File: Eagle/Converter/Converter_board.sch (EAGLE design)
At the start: 9 parts

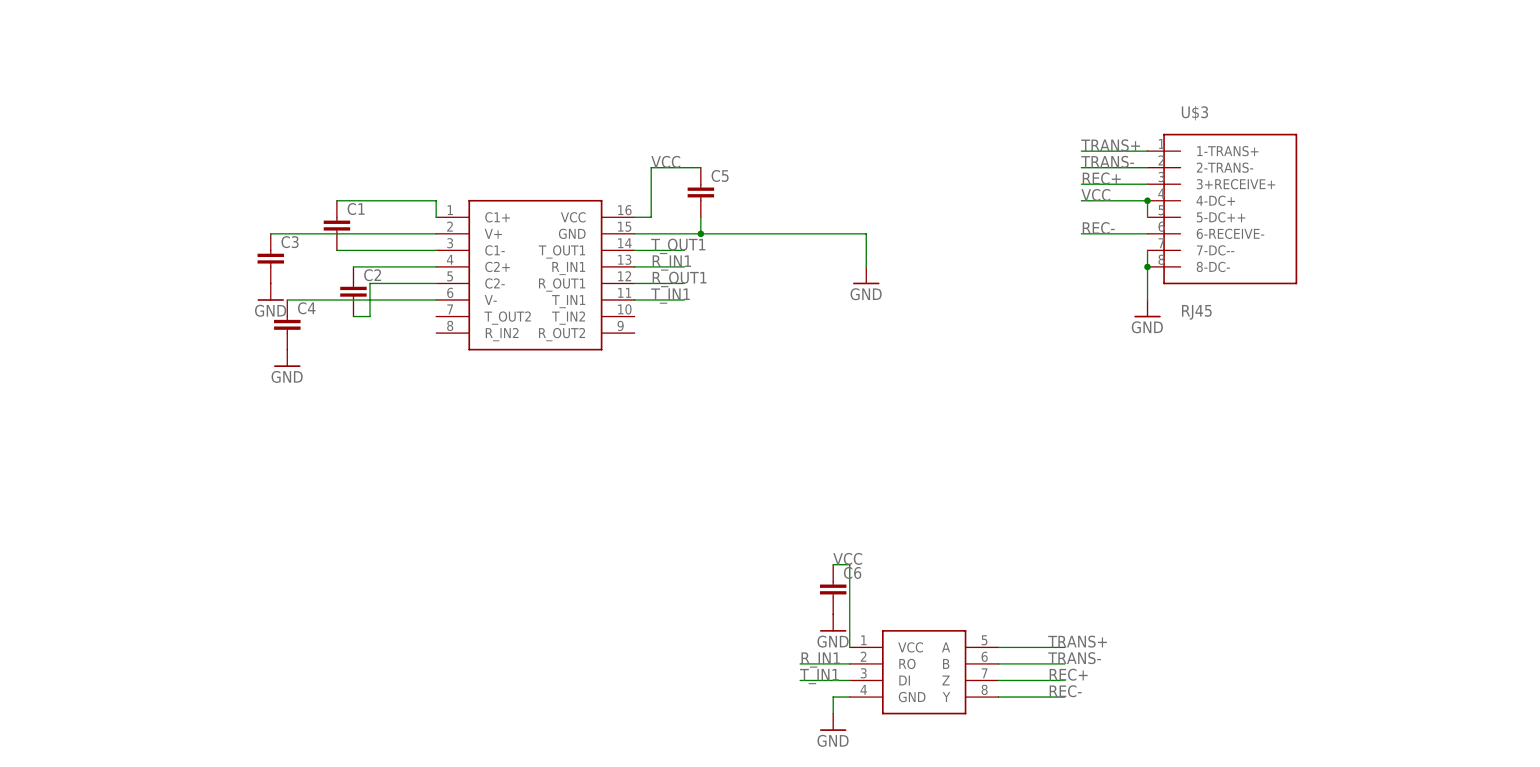
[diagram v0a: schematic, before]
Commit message: Added all parts needed
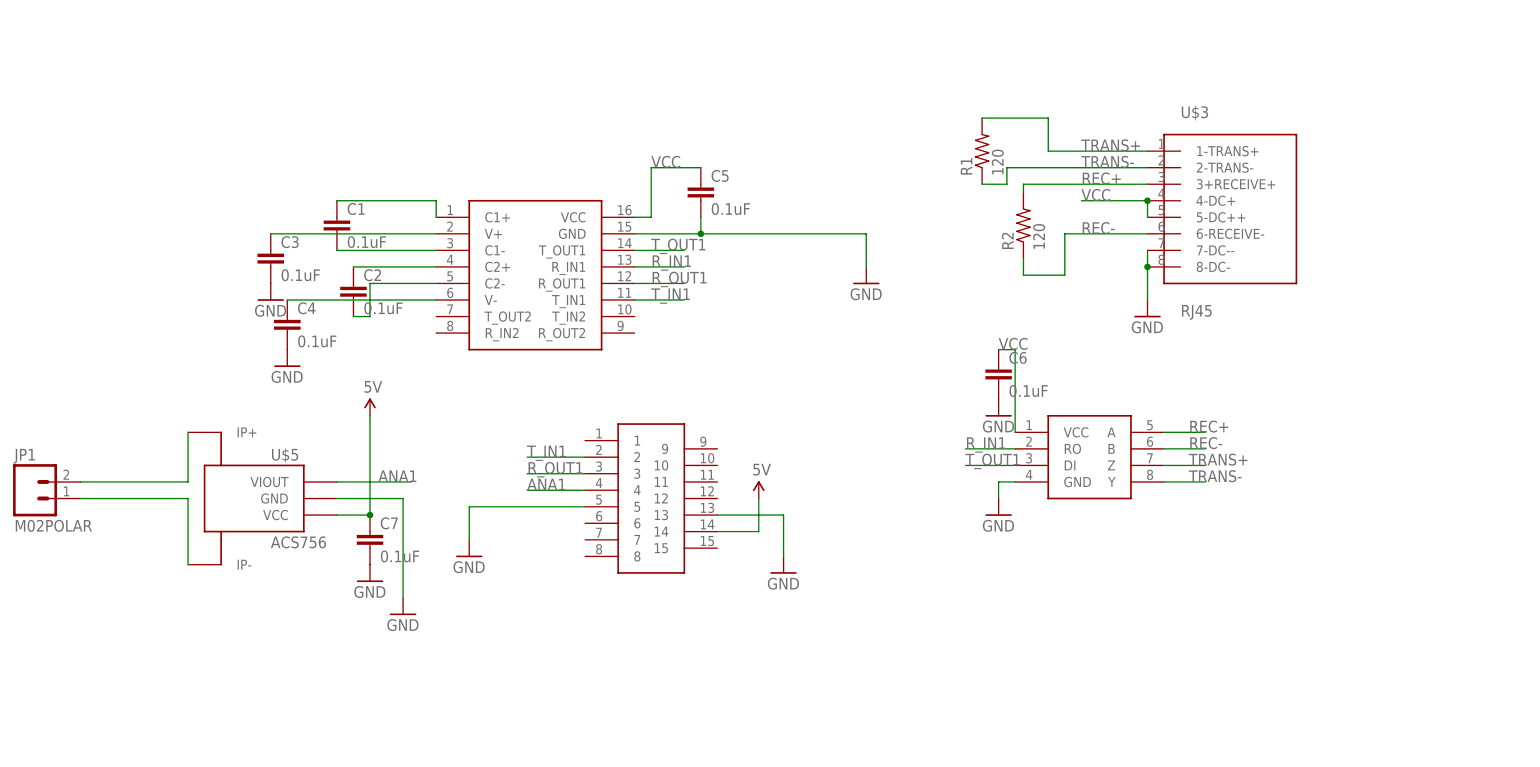
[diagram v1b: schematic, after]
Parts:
- added C7: 0.1uF, SparkFun-Capacitors:CAP1206
- added JP1: M02POLAR, SparkFun-Connectors:M02POLAR
- added R1, R2: 120, SparkFun-Passives:RESISTOR1206
- added U$4: DB15, MRDT-LIB2014:DB15
- added U$5: ACS756, MRDT-2015-BMS:ACS770
- C1, C2, C3, C4, C5, C6: value (none) -> 0.1uF
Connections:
- new net ANA1: U$4.4, U$5.VIOUT
- new net N$7: JP1.2, U$5.IP+
- new net N$9: JP1.1, U$5.IP-
- net GND: now also C7.2, U$4.13, U$4.5, U$5.GND
- net REC+: now also R2.2, U$1.A; no longer U$1.Z
- net REC-: now also R2.1, U$1.B; no longer U$1.Y
- net R_OUT1: now also U$4.3
- net TRANS+: now also R1.2, U$1.Z; no longer U$1.A
- net TRANS-: now also R1.1, U$1.Y; no longer U$1.B
- net T_IN1: now also U$4.2; no longer U$1.DI
- net T_OUT1: now also U$1.DI
- net VCC: now also C7.1, U$4.14, U$5.VCC
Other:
- moved on the sheet: C6

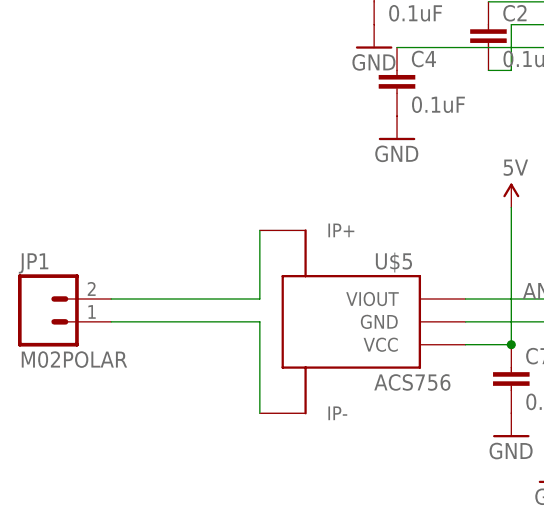
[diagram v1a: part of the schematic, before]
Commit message: Finished Schematic, Setup Board Layout. Waiting to hear final decision on Torque control.
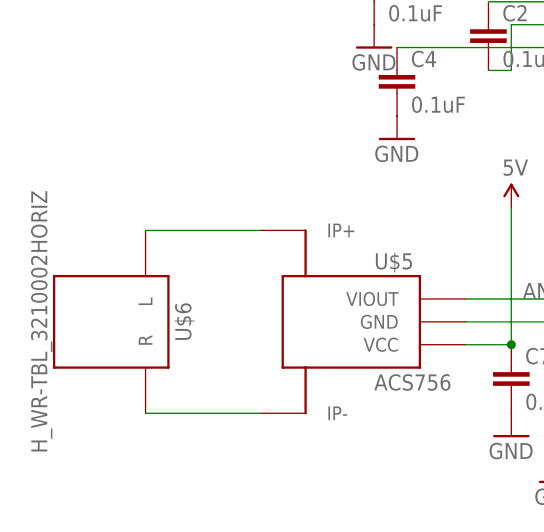
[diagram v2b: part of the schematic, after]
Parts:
- removed JP1: M02POLAR, SparkFun-Connectors:M02POLAR
- added U$6: H_WR-TBL_3210002HORIZ, MRDT-2015-PowerBoard:H_WR-TBL_3210002HORIZ
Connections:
- removed net N$9: JP1.1, U$5.IP-
- new net N$8: U$5.IP-, U$6.R
- net N$7: now also U$6.L; no longer JP1.2
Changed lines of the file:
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@@
 <part name="GND9" library="SparkFun-Aesthetics" deviceset="GND" device=""/>
 <part name="VCC1" library="SparkFun-Aesthetics" deviceset="5V" device=""/>
-<part name="JP1" library="SparkFun-Connectors" deviceset="M02" device="POLAR"/>
 <part name="R1" library="SparkFun-Passives" deviceset="RESISTOR" device="1206" value="120"/>
 <part name="R2" library="SparkFun-Passives" deviceset="RESISTOR" device="1206" value="120"/>
 <part name="C7" library="SparkFun-Capacitors" deviceset="CAP" device="1206" value="0.1uF"/>
 <part name="GND10" library="SparkFun-Aesthetics" deviceset="GND" device=""/>
+<part name="U$6" library="MRDT-2015-PowerBoard" deviceset="H_WR-TBL_32*1*0002" device="HORIZ"/>
 </parts>
 <sheets>
@@
 <instance part="GND9" gate="1" x="-15.24" y="45.72"/>
 <instance part="VCC1" gate="G$1" x="-20.32" y="76.2"/>
-<instance part="JP1" gate="G$1" x="-72.39" y="63.5"/>
 <instance part="R1" gate="G$1" x="73.66" y="116.84" rot="R90"/>
 <instance part="R2" gate="G$1" x="80.01" y="105.41" rot="R90"/>
 <instance part="C7" gate="G$1" x="-20.32" y="55.88"/>
 <instance part="GND10" gate="1" x="-20.32" y="50.8"/>
+<instance part="U$6" gate="G$1" x="-63.5" y="63.5" rot="R270"/>
 </instances>
 <busses>
@@
 <net name="N$7" class="0">
 <segment>
-<pinref part="JP1" gate="G$1" pin="2"/>
 <pinref part="U$5" gate="G$1" pin="IP+"/>
-<wire x1="-64.77" y1="66.04" x2="-48.26" y2="66.04" width="0.1524" layer="91"/>
-<wire x1="-48.26" y1="66.04" x2="-48.26" y2="73.66" width="0.1524" layer="91"/>
-</segment>
-</net>
-<net name="N$9" class="0">
-<segment>
-<pinref part="JP1" gate="G$1" pin="1"/>
+<wire x1="-48.26" y1="73.66" x2="-60.96" y2="73.66" width="0.1524" layer="91"/>
+<pinref part="U$6" gate="G$1" pin="L"/>
+</segment>
+</net>
+<net name="N$8" class="0">
+<segment>
 <pinref part="U$5" gate="G$1" pin="IP-"/>
-<wire x1="-64.77" y1="63.5" x2="-48.26" y2="63.5" width="0.1524" layer="91"/>
-<wire x1="-48.26" y1="63.5" x2="-48.26" y2="53.34" width="0.1524" layer="91"/>
-</segment>
-</net>
+<wire x1="-48.26" y1="53.34" x2="-60.96" y2="53.34" width="0.1524" layer="91"/>
+<pinref part="U$6" gate="G$1" pin="R"/>
+</segment>
+</net>

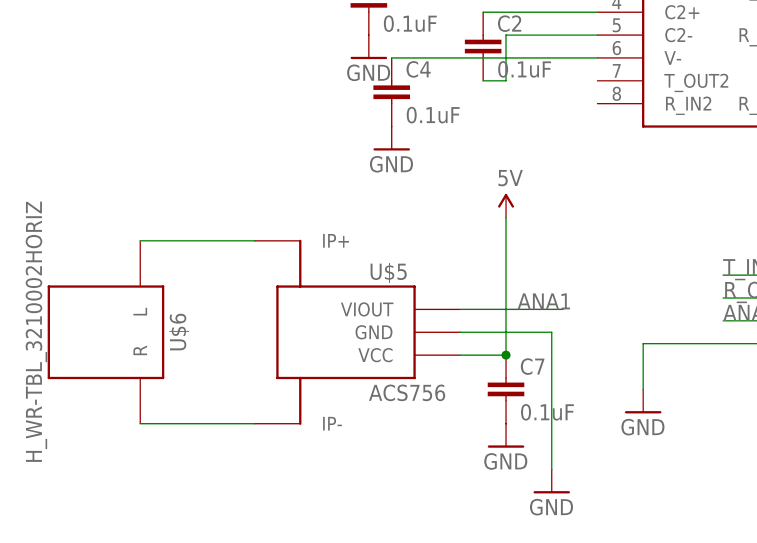
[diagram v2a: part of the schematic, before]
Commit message: Removed the Current Sensor. No more Torque control.
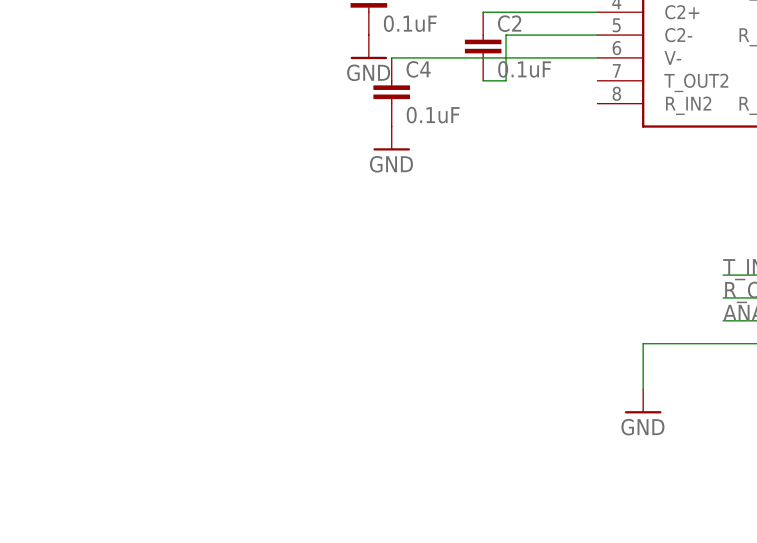
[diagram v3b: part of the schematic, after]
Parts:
- removed C7: 0.1uF, SparkFun-Capacitors:CAP1206
- removed U$5: ACS756, MRDT-2015-BMS:ACS770
- removed U$6: H_WR-TBL_3210002HORIZ, MRDT-2015-PowerBoard:H_WR-TBL_3210002HORIZ
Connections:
- removed net N$7: U$5.IP+, U$6.L
- removed net N$8: U$5.IP-, U$6.R
- net ANA1: no longer U$5.VIOUT
- net GND: no longer C7.2, U$5.GND
- net VCC: no longer C7.1, U$5.VCC
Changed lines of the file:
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@@
 <part name="GND8" library="SparkFun-Aesthetics" deviceset="GND" device=""/>
 <part name="VCC" library="SparkFun-Aesthetics" deviceset="5V" device=""/>
-<part name="U$5" library="MRDT-2015-BMS" deviceset="ACS770" device="" value="ACS756"/>
-<part name="GND9" library="SparkFun-Aesthetics" deviceset="GND" device=""/>
-<part name="VCC1" library="SparkFun-Aesthetics" deviceset="5V" device=""/>
 <part name="R1" library="SparkFun-Passives" deviceset="RESISTOR" device="1206" value="120"/>
 <part name="R2" library="SparkFun-Passives" deviceset="RESISTOR" device="1206" value="120"/>
-<part name="C7" library="SparkFun-Capacitors" deviceset="CAP" device="1206" value="0.1uF"/>
-<part name="GND10" library="SparkFun-Aesthetics" deviceset="GND" device=""/>
-<part name="U$6" library="MRDT-2015-PowerBoard" deviceset="H_WR-TBL_32*1*0002" device="HORIZ"/>
 </parts>
 <sheets>
@@
 <instance part="GND8" gate="1" x="-5.08" y="54.61"/>
 <instance part="VCC" gate="G$1" x="39.37" y="63.5"/>
-<instance part="U$5" gate="G$1" x="-38.1" y="63.5"/>
-<instance part="GND9" gate="1" x="-15.24" y="45.72"/>
-<instance part="VCC1" gate="G$1" x="-20.32" y="76.2"/>
 <instance part="R1" gate="G$1" x="73.66" y="116.84" rot="R90"/>
 <instance part="R2" gate="G$1" x="80.01" y="105.41" rot="R90"/>
-<instance part="C7" gate="G$1" x="-20.32" y="55.88"/>
-<instance part="GND10" gate="1" x="-20.32" y="50.8"/>
-<instance part="U$6" gate="G$1" x="-63.5" y="63.5" rot="R270"/>
 </instances>
 <busses>
@@
 <pinref part="GND8" gate="1" pin="GND"/>
 </segment>
-<segment>
-<pinref part="U$5" gate="G$1" pin="GND"/>
-<wire x1="-25.4" y1="63.5" x2="-15.24" y2="63.5" width="0.1524" layer="91"/>
-<wire x1="-15.24" y1="63.5" x2="-15.24" y2="48.26" width="0.1524" layer="91"/>
-<pinref part="GND9" gate="1" pin="GND"/>
-</segment>
-<segment>
-<pinref part="C7" gate="G$1" pin="2"/>
-<pinref part="GND10" gate="1" pin="GND"/>
-</segment>
 </net>
 <net name="VCC" class="0">
@@
 <wire x1="39.37" y1="58.42" x2="39.37" y2="63.5" width="0.1524" layer="91"/>
 <pinref part="VCC" gate="G$1" pin="5V"/>
-</segment>
-<segment>
-<pinref part="U$5" gate="G$1" pin="VCC"/>
-<wire x1="-25.4" y1="60.96" x2="-20.32" y2="60.96" width="0.1524" layer="91"/>
-<wire x1="-20.32" y1="60.96" x2="-20.32" y2="76.2" width="0.1524" layer="91"/>
-<pinref part="VCC1" gate="G$1" pin="5V"/>
-<pinref part="C7" gate="G$1" pin="1"/>
-<junction x="-20.32" y="60.96"/>
 </segment>
 </net>
@@
 <label x="3.81" y="64.77" size="1.778" layer="95"/>
 </segment>
-<segment>
-<pinref part="U$5" gate="G$1" pin="VIOUT"/>
-<wire x1="-25.4" y1="66.04" x2="-13.97" y2="66.04" width="0.1524" layer="91"/>
-<label x="-19.05" y="66.04" size="1.778" layer="95"/>
-</segment>
-</net>
-<net name="N$7" class="0">
-<segment>
-<pinref part="U$5" gate="G$1" pin="IP+"/>
-<wire x1="-48.26" y1="73.66" x2="-60.96" y2="73.66" width="0.1524" layer="91"/>
-<pinref part="U$6" gate="G$1" pin="L"/>
-</segment>
-</net>
-<net name="N$8" class="0">
-<segment>
-<pinref part="U$5" gate="G$1" pin="IP-"/>
-<wire x1="-48.26" y1="53.34" x2="-60.96" y2="53.34" width="0.1524" layer="91"/>
-<pinref part="U$6" gate="G$1" pin="R"/>
-</segment>
-</net>
+</net>

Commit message: Updated
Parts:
- added JP1: M02POLAR, SparkFun-Connectors:M02POLAR
- added U1: MAX232SOIC16, SparkFun-DigitalIC:MAX232SOIC16
- U$2: value MAX3232 -> V_REG_MIC2920; device MRDT-LIB2014:MAX3232 -> SparkFun-PowerIC:V_REG_MIC2920
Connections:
- removed net ANA1: U$4.4
- removed net R_IN1: U$1.RO, U$2.R_IN1
- removed net R_OUT1: U$2.R_OUT1, U$4.3
- removed net T_IN1: U$2.T_IN1, U$4.2
- removed net T_OUT1: U$1.DI, U$2.T_OUT1
- new net 3P3V: C6.1, U$1.VCC, U$2.OUT
- new net RS232_FROM_MOBO: U$4.3, U1.T1OUT
- new net RS232_TO_MOBO: U$4.2, U1.R1IN
- new net TTL_FROM_MOBO: U$1.RO, U1.T1IN
- new net TTL_TO_MOBO: U$1.DI, U1.R1OUT
- net GND: now also C1.2, C2.2, JP1.1, U1.GND; no longer C3.2, C4.2
- net N$1: now also C2.1, U1.V-; no longer C1.2, U$2.C1-
- net N$2: now also U1.V+; no longer U$2.C1+
- net N$3: now also C3.1, U1.C1+; no longer C2.1, U$2.C2+
- net N$4: now also C3.2, U1.C1-; no longer C2.2, U$2.C2-
- net N$5: now also U1.C2+; no longer U$2.V-
- net N$6: now also C4.2, U1.C2-; no longer C3.1, U$2.V+
- net VCC: now also JP1.2, U$2.IN, U1.VCC; no longer C6.1, U$1.VCC, U$2.VCC, U$4.14
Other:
- note added: "add tx and rx leds"
- note added: "fix both 5v supply problem"
- moved on the sheet: C1, C2, C3, C4, C5
